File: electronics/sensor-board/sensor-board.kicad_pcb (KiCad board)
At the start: 0 parts

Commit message: Added libraries to sensor board pcb schematic
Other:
- copper layers 0 -> 2
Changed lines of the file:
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@@
-(kicad_pcb (version 20210722) (generator pcbnew)
+(kicad_pcb (version 20210824) (generator pcbnew)
+  (general
+    (thickness 1.6)
+  )
+  (paper "A4")
+  (layers
+    (0 "F.Cu" signal)
+    (31 "B.Cu" signal)
+    (32 "B.Adhes" user "B.Adhesive")
+    (33 "F.Adhes" user "F.Adhesive")
+    (34 "B.Paste" user)
+    (35 "F.Paste" user)
+    (36 "B.SilkS" user "B.Silkscreen")
+    (37 "F.SilkS" user "F.Silkscreen")
+    (38 "B.Mask" user)
+    (39 "F.Mask" user)
+    (40 "Dwgs.User" user "User.Drawings")
+    (41 "Cmts.User" user "User.Comments")
+    (42 "Eco1.User" user "User.Eco1")
+    (43 "Eco2.User" user "User.Eco2")
+    (44 "Edge.Cuts" user)
+    (45 "Margin" user)
+    (46 "B.CrtYd" user "B.Courtyard")
+    (47 "F.CrtYd" user "F.Courtyard")
+    (48 "B.Fab" user)
+    (49 "F.Fab" user)
+    (50 "User.1" user)
+    (51 "User.2" user)
+    (52 "User.3" user)
+    (53 "User.4" user)
+    (54 "User.5" user)
+    (55 "User.6" user)
+    (56 "User.7" user)
+    (57 "User.8" user)
+    (58 "User.9" user)
+  )
+  (setup
+    (pad_to_mask_clearance 0)
+    (pcbplotparams
+      (layerselection 0x00010fc_ffffffff)
+      (disableapertmacros false)
+      (usegerberextensions false)
+      (usegerberattributes true)
+      (usegerberadvancedattributes true)
+      (creategerberjobfile true)
+      (svguseinch false)
+      (svgprecision 6)
+      (excludeedgelayer true)
+      (plotframeref false)
+      (viasonmask false)
+      (mode 1)
+      (useauxorigin false)
+      (hpglpennumber 1)
+      (hpglpenspeed 20)
+      (hpglpendiameter 15.000000)
+      (dxfpolygonmode true)
+      (dxfimperialunits true)
+      (dxfusepcbnewfont true)
+      (psnegative false)
+      (psa4output false)
+      (plotreference true)
+      (plotvalue true)
+      (plotinvisibletext false)
+      (sketchpadsonfab false)
+      (subtractmaskfromsilk false)
+      (outputformat 1)
+      (mirror false)
+      (drillshape 1)
+      (scaleselection 1)
+      (outputdirectory "")
+    )
+  )
+  (net 0 "")
 )

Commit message: work on sensor-board
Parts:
- added C1: 1uF, Capacitor_SMD:C_0603_1608Metric, F.Cu at (64.9, -87.0)
- added C10: 100nF, Capacitor_SMD:C_0603_1608Metric, F.Cu at (230.6, -32.4)
- added C11: 100nF, Capacitor_SMD:C_0603_1608Metric, F.Cu at (237.2, -24.8)
- added C12: 20pF, Capacitor_SMD:C_0603_1608Metric, F.Cu at (181.7, 95.5)
- added C13: 0.1uF, Capacitor_SMD:C_0603_1608Metric, F.Cu at (-39.4, 22.1)
- added C14: 0.1uF, Capacitor_SMD:C_0603_1608Metric, F.Cu at (-42.3, 93.4)
- added C15: 0.1uF, Capacitor_SMD:C_0603_1608Metric, F.Cu at (-38.2, 22.2)
- added C16: 0.1uF, Capacitor_SMD:C_0603_1608Metric, F.Cu at (-42.6, 94.6)
- added C17: 0.1uF, Capacitor_SMD:C_0603_1608Metric, F.Cu at (-38.1, 167.5)
- added C18: 0.1uF, Capacitor_SMD:C_0603_1608Metric, F.Cu at (-30.2, 42.9)
- added C19: 0.1uF, Capacitor_SMD:C_0603_1608Metric, F.Cu at (-34.6, 118.8)
- added C2: 10nF, Capacitor_SMD:C_0603_1608Metric, F.Cu at (57.4, -80.2)
- added C20: 0.1uF, Capacitor_SMD:C_0603_1608Metric, F.Cu at (-37.3, 168.5)
- added C21: 0.1uF, Capacitor_SMD:C_0603_1608Metric, F.Cu at (-31.4, 42.1)
- added C22: 0.1uF, Capacitor_SMD:C_0603_1608Metric, F.Cu at (-36.1, 117.2)
- added C23: 0.1uF, Capacitor_SMD:C_0603_1608Metric, F.Cu at (-38.1, 65.0)
- added C24: 0.1uF, Capacitor_SMD:C_0603_1608Metric, F.Cu at (-36.8, 141.4)
- added C25: 0.1uF, Capacitor_SMD:C_0603_1608Metric, F.Cu at (-39.3, 65.0)
- added C26: 0.1uF, Capacitor_SMD:C_0603_1608Metric, F.Cu at (-39.0, 141.4)
- added C27: 20pF, Capacitor_SMD:C_0603_1608Metric, F.Cu at (175.1, 101.0)
- added C28: 100nF, Capacitor_SMD:C_0603_1608Metric, F.Cu at (160.2, 53.9)
- added C29: 100nF, Capacitor_SMD:C_0603_1608Metric, F.Cu at (245.2, -24.1)
- added C3: 1uF, Capacitor_SMD:C_0603_1608Metric, F.Cu at (64.8, -80.0)
- added C6: 100nF, Capacitor_SMD:C_0603_1608Metric, F.Cu at (201.7, -32.7)
- added C7: 100nF, Capacitor_SMD:C_0603_1608Metric, F.Cu at (214.6, -31.9)
- added C8: 100nF, Capacitor_SMD:C_0603_1608Metric, F.Cu at (164.4, 147.2)
- added C9: 100nF, Capacitor_SMD:C_0603_1608Metric, F.Cu at (223.1, -30.6)
- added J1: SWD Header, Connector_PinHeader_2.54mm:PinHeader_1x04_P2.54mm_Vertical, F.Cu at (305.6, -41.4)
- added J10: Suppply_5V, Connector_PinHeader_2.54mm:PinHeader_1x02_P2.54mm_Horizontal, F.Cu at (79.5, -82.9)
- added J11: Pressure_1, Connector_PinHeader_2.54mm:PinHeader_1x02_P2.54mm_Horizontal, F.Cu at (199.5, 360.1)
- added J12: Pressure_2, Connector_PinHeader_2.54mm:PinHeader_1x02_P2.54mm_Horizontal, F.Cu at (189.3, 360.6)
- added J13: Pressure_3, Connector_PinHeader_2.54mm:PinHeader_1x02_P2.54mm_Horizontal, F.Cu at (179.7, 361.2)
- added J14: Pressure_4, Connector_PinHeader_2.54mm:PinHeader_1x02_P2.54mm_Horizontal, F.Cu at (168.6, 362.4)
- added J15: Pressure_9, Connector_PinHeader_2.54mm:PinHeader_1x02_P2.54mm_Horizontal, F.Cu at (110.0, 366.5)
- added J16: Flow_1, Connector_PinHeader_2.54mm:PinHeader_1x04_P2.54mm_Horizontal, F.Cu at (66.5, 365.6)
- added J17: Flow_2, Connector_PinHeader_2.54mm:PinHeader_1x04_P2.54mm_Horizontal, F.Cu at (93.5, 364.6)
- added J18: CAN_Bus, Resistor_THT:R_Axial_DIN0204_L3.6mm_D1.6mm_P1.90mm_Vertical, F.Cu at (324.9, 28.0)
- added J19: Spare_1, Connector_PinHeader_2.54mm:PinHeader_1x02_P2.54mm_Horizontal, F.Cu at (268.7, 356.6)
- added J2: Supply_24V, Connector_PinHeader_2.54mm:PinHeader_1x02_P2.54mm_Horizontal, F.Cu at (88.4, -34.7)
- added J20: Spare_2, Connector_PinHeader_2.54mm:PinHeader_1x02_P2.54mm_Horizontal, F.Cu at (252.9, 358.1)
- added J21: Spare_3, Connector_PinHeader_2.54mm:PinHeader_1x02_P2.54mm_Horizontal, F.Cu at (236.7, 359.6)
- added J22: Spare_4, Connector_PinHeader_2.54mm:PinHeader_1x02_P2.54mm_Horizontal, F.Cu at (223.0, 361.2)
- added J23: Therm_1, K_type_thermo_conn_F:K_type_thermo_conn_F, F.Cu at (-62.7, 20.7)
- added J24: Therm_4, K_type_thermo_conn_F:K_type_thermo_conn_F, F.Cu at (-62.4, 93.3)
- added J25: Therm_7, K_type_thermo_conn_F:K_type_thermo_conn_F, F.Cu at (-62.4, 169.5)
- added J26: Therm_2, K_type_thermo_conn_F:K_type_thermo_conn_F, F.Cu at (-62.4, 42.5)
- added J27: Therm_5, K_type_thermo_conn_F:K_type_thermo_conn_F, F.Cu at (-62.4, 118.7)
- added J28: Therm_3, K_type_thermo_conn_F:K_type_thermo_conn_F, F.Cu at (-61.4, 67.9)
- added J29: Therm_6, K_type_thermo_conn_F:K_type_thermo_conn_F, F.Cu at (-62.4, 144.1)
- added J3: Supply_12V, Connector_PinHeader_2.54mm:PinHeader_1x02_P2.54mm_Horizontal, F.Cu at (85.4, -57.3)
- added J30: Spare_HR, Connector_PinHeader_2.54mm:PinHeader_1x04_P2.54mm_Horizontal, F.Cu at (450.2, 241.1)
- added J4: Load_C_1, Connector_PinHeader_2.54mm:PinHeader_1x04_P2.54mm_Horizontal, F.Cu at (443.0, 163.0)
- added J5: Load_C_2, Connector_PinHeader_2.54mm:PinHeader_1x04_P2.54mm_Horizontal, F.Cu at (436.7, 202.7)
- added J6: Pressure_5, Connector_PinHeader_2.54mm:PinHeader_1x02_P2.54mm_Horizontal, F.Cu at (159.3, 363.2)
- added J7: Pressure_6, Connector_PinHeader_2.54mm:PinHeader_1x02_P2.54mm_Horizontal, F.Cu at (149.0, 363.8)
- added J8: Pressure_7, Connector_PinHeader_2.54mm:PinHeader_1x02_P2.54mm_Horizontal, F.Cu at (137.3, 364.9)
- added J9: Pressure_8, Connector_PinHeader_2.54mm:PinHeader_1x02_P2.54mm_Horizontal, F.Cu at (123.1, 364.8)
- added L1: 10uH, Inductor_SMD:L_0603_1608Metric, F.Cu at (156.8, 147.4)
- added R10: 100, Resistor_SMD:R_0603_1608Metric, F.Cu at (-41.6, 22.8)
- added R100: 150, Resistor_SMD:R_0603_1608Metric, F.Cu at (87.3, 356.7)
- added R101: NO_RES, Resistor_SMD:R_0603_1608Metric, F.Cu at (33.2, 336.4)
- added R102: 150, Resistor_SMD:R_0603_1608Metric, F.Cu at (106.1, 357.0)
- added R103: 150, Resistor_SMD:R_0603_1608Metric, F.Cu at (64.1, 348.0)
- added R104: 150, Resistor_SMD:R_0603_1608Metric, F.Cu at (87.5, 346.4)
- added R105: NO_RES, Resistor_SMD:R_0603_1608Metric, F.Cu at (39.5, 327.5)
- added R106: NO_RES, Resistor_SMD:R_0603_1608Metric, F.Cu at (43.4, 342.7)
- added R107: NO_RES, Resistor_SMD:R_0603_1608Metric, F.Cu at (37.1, 321.0)
- added R108: TO CALCULATE 4.7k, Resistor_SMD:R_0603_1608Metric, F.Cu at (321.4, 80.5)
- added R109: 100, Resistor_SMD:R_0603_1608Metric, F.Cu at (317.4, 83.0)
- added R11: 100, Resistor_SMD:R_0603_1608Metric, F.Cu at (-40.5, 94.5)
- added R110: 100, Resistor_SMD:R_0603_1608Metric, F.Cu at (325.4, 77.9)
- added R111: 10k, Resistor_SMD:R_0603_1608Metric, F.Cu at (164.1, 121.9)
- added R112: 0k, Resistor_SMD:R_0603_1608Metric, F.Cu at (168.7, 104.6)
- added R12: 100, Resistor_SMD:R_0603_1608Metric, F.Cu at (-41.6, 94.1)
- added R13: 10k, Resistor_SMD:R_0603_1608Metric, F.Cu at (-41.3, 93.6)
- added R14: 7.5k, Resistor_SMD:R_0603_1608Metric, F.Cu at (-42.1, 93.8)
- added R15: 2M, Resistor_SMD:R_0603_1608Metric, F.Cu at (-38.7, 168.3)
- added R16: 2M, Resistor_SMD:R_0603_1608Metric, F.Cu at (-38.3, 168.8)
- added R17: 1M, Resistor_SMD:R_0603_1608Metric, F.Cu at (-38.7, 167.9)
- added R18: 100, Resistor_SMD:R_0603_1608Metric, F.Cu at (-39.7, 168.5)
- added R19: 100, Resistor_SMD:R_0603_1608Metric, F.Cu at (-39.3, 169.2)
- added R2: TO CALCULATE 4.7k, Resistor_SMD:R_0603_1608Metric, F.Cu at (315.4, 73.8)
- added R20: 2M, Resistor_SMD:R_0603_1608Metric, F.Cu at (-31.6, 41.7)
- added R21: 2M, Resistor_SMD:R_0603_1608Metric, F.Cu at (-36.1, 117.8)
- added R22: 2M, Resistor_SMD:R_0603_1608Metric, F.Cu at (-30.6, 42.0)
- added R23: 2M, Resistor_SMD:R_0603_1608Metric, F.Cu at (-36.7, 117.2)
- added R24: 1M, Resistor_SMD:R_0603_1608Metric, F.Cu at (-30.8, 41.5)
- added R25: 1M, Resistor_SMD:R_0603_1608Metric, F.Cu at (-36.7, 117.6)
- added R26: 100, Resistor_SMD:R_0603_1608Metric, F.Cu at (-32.1, 41.9)
- added R27: 100, Resistor_SMD:R_0603_1608Metric, F.Cu at (-30.6, 42.4)
- added R28: 100, Resistor_SMD:R_0603_1608Metric, F.Cu at (-37.5, 116.3)
- added R29: 100, Resistor_SMD:R_0603_1608Metric, F.Cu at (-35.9, 118.8)
- added R3: 2M, Resistor_SMD:R_0603_1608Metric, F.Cu at (-35.9, 22.3)
- added R30: 10k, Resistor_SMD:R_0603_1608Metric, F.Cu at (-39.1, 167.7)
- added R31: 43k, Resistor_SMD:R_0603_1608Metric, F.Cu at (-40.8, 166.6)
- added R32: 10k, Resistor_SMD:R_0603_1608Metric, F.Cu at (-30.8, 42.7)
- added R33: 10k, Resistor_SMD:R_0603_1608Metric, F.Cu at (-36.8, 116.2)
- added R34: 2.2k, Resistor_SMD:R_0603_1608Metric, F.Cu at (-31.5, 42.1)
- added R35: 13k, Resistor_SMD:R_0603_1608Metric, F.Cu at (-36.8, 116.2)
- added R36: 2M, Resistor_SMD:R_0603_1608Metric, F.Cu at (-40.1, 64.9)
- added R37: 2M, Resistor_SMD:R_0603_1608Metric, F.Cu at (-36.5, 140.5)
- added R38: 2M, Resistor_SMD:R_0603_1608Metric, F.Cu at (-39.6, 64.8)
- added R39: 2M, Resistor_SMD:R_0603_1608Metric, F.Cu at (-37.7, 143.1)
- added R4: 2M, Resistor_SMD:R_0603_1608Metric, F.Cu at (-42.4, 94.1)
- added R40: 1M, Resistor_SMD:R_0603_1608Metric, F.Cu at (-39.6, 64.5)
- added R41: 1M, Resistor_SMD:R_0603_1608Metric, F.Cu at (-37.4, 142.2)
- added R42: 100, Resistor_SMD:R_0603_1608Metric, F.Cu at (-39.1, 64.4)
- added R43: 100, Resistor_SMD:R_0603_1608Metric, F.Cu at (-39.9, 65.5)
- added R44: 100, Resistor_SMD:R_0603_1608Metric, F.Cu at (-39.4, 140.5)
- added R45: 100, Resistor_SMD:R_0603_1608Metric, F.Cu at (-38.8, 143.4)
- added R46: 10k, Resistor_SMD:R_0603_1608Metric, F.Cu at (-37.6, 64.9)
- added R47: 10k, Resistor_SMD:R_0603_1608Metric, F.Cu at (-38.2, 142.2)
- added R48: 4.3k, Resistor_SMD:R_0603_1608Metric, F.Cu at (-40.4, 63.9)
- added R49: 22k, Resistor_SMD:R_0603_1608Metric, F.Cu at (-39.6, 142.8)
- added R5: 2M, Resistor_SMD:R_0603_1608Metric, F.Cu at (-39.2, 22.4)
- added R50: NO_RES, Resistor_SMD:R_0603_1608Metric, F.Cu at (269.4, 349.2)
- added R51: NO_RES, Resistor_SMD:R_0603_1608Metric, F.Cu at (264.3, 350.7)
- added R52: NO_RES, Resistor_SMD:R_0603_1608Metric, F.Cu at (254.5, 346.9)
- added R53: NO_RES, Resistor_SMD:R_0603_1608Metric, F.Cu at (250.2, 349.8)
- added R54: NO_RES, Resistor_SMD:R_0603_1608Metric, F.Cu at (238.2, 349.7)
- added R55: NO_RES, Resistor_SMD:R_0603_1608Metric, F.Cu at (233.4, 352.9)
- added R56: NO_RES, Resistor_SMD:R_0603_1608Metric, F.Cu at (224.4, 353.2)
- added R57: NO_RES, Resistor_SMD:R_0603_1608Metric, F.Cu at (220.2, 352.9)
- added R58: NO_RES, Resistor_SMD:R_0603_1608Metric, F.Cu at (264.0, 340.8)
- added R59: NO_RES, Resistor_SMD:R_0603_1608Metric, F.Cu at (249.7, 336.0)
- added R6: 2M, Resistor_SMD:R_0603_1608Metric, F.Cu at (-41.3, 94.7)
- added R60: NO_RES, Resistor_SMD:R_0603_1608Metric, F.Cu at (233.6, 340.9)
- added R61: NO_RES, Resistor_SMD:R_0603_1608Metric, F.Cu at (220.7, 339.9)
- added R62: NO_RES, Resistor_SMD:R_0603_1608Metric, F.Cu at (231.4, 302.6)
- added R63: NO_RES, Resistor_SMD:R_0603_1608Metric, F.Cu at (244.3, 318.6)
- added R64: NO_RES, Resistor_SMD:R_0603_1608Metric, F.Cu at (234.6, 314.8)
- added R65: NO_RES, Resistor_SMD:R_0603_1608Metric, F.Cu at (219.0, 308.2)
- added R66: 100, Resistor_SMD:R_0603_1608Metric, F.Cu at (425.0, 208.4)
- added R67: 24.92, Resistor_SMD:R_0603_1608Metric, F.Cu at (425.8, 200.5)
- added R68: 100, Resistor_SMD:R_0603_1608Metric, F.Cu at (430.6, 167.1)
- added R69: 24.92, Resistor_SMD:R_0603_1608Metric, F.Cu at (425.2, 163.2)
- added R7: 1M, Resistor_SMD:R_0603_1608Metric, F.Cu at (-31.2, 22.3)
- added R70: 100, Resistor_SMD:R_0603_1608Metric, F.Cu at (417.4, 255.7)
- added R71: 24.92, Resistor_SMD:R_0603_1608Metric, F.Cu at (423.3, 248.1)
- added R72: 100, Resistor_SMD:R_0603_1608Metric, F.Cu at (422.8, 326.6)
- added R73: 24.92, Resistor_SMD:R_0603_1608Metric, F.Cu at (425.5, 347.3)
- added R74: 82500, Resistor_SMD:R_0603_1608Metric, F.Cu at (431.1, 206.7)
- added R75: 82500, Resistor_SMD:R_0603_1608Metric, F.Cu at (430.0, 257.6)
- added R76: 82500, Resistor_SMD:R_0603_1608Metric, F.Cu at (416.2, 171.4)
- added R77: 82500, Resistor_SMD:R_0603_1608Metric, F.Cu at (431.4, 343.5)
- added R78: 82500, Resistor_SMD:R_0603_1608Metric, F.Cu at (414.5, 161.6)
- added R79: 82500, Resistor_SMD:R_0603_1608Metric, F.Cu at (409.3, 205.4)
- added R8: 1M, Resistor_SMD:R_0603_1608Metric, F.Cu at (-42.0, 93.6)
- added R80: 82500, Resistor_SMD:R_0603_1608Metric, F.Cu at (431.3, 243.3)
- added R81: 82500, Resistor_SMD:R_0603_1608Metric, F.Cu at (402.4, 339.2)
- added R82: 150, Resistor_SMD:R_0603_1608Metric, F.Cu at (195.3, 354.5)
- added R83: 150, Resistor_SMD:R_0603_1608Metric, F.Cu at (185.9, 355.8)
- added R84: 150, Resistor_SMD:R_0603_1608Metric, F.Cu at (175.9, 355.0)
- added R85: 150, Resistor_SMD:R_0603_1608Metric, F.Cu at (165.5, 358.8)
- added R86: 150, Resistor_SMD:R_0603_1608Metric, F.Cu at (195.3, 342.5)
- added R87: 150, Resistor_SMD:R_0603_1608Metric, F.Cu at (186.0, 346.2)
- added R88: 150, Resistor_SMD:R_0603_1608Metric, F.Cu at (175.2, 346.4)
- added R89: 150, Resistor_SMD:R_0603_1608Metric, F.Cu at (165.9, 347.3)
- added R9: 100, Resistor_SMD:R_0603_1608Metric, F.Cu at (-39.7, 21.8)
- added R90: 150, Resistor_SMD:R_0603_1608Metric, F.Cu at (156.6, 356.0)
- added R91: 150, Resistor_SMD:R_0603_1608Metric, F.Cu at (146.7, 356.1)
- added R92: 150, Resistor_SMD:R_0603_1608Metric, F.Cu at (134.4, 357.9)
- added R93: 150, Resistor_SMD:R_0603_1608Metric, F.Cu at (120.3, 359.8)
- added R94: 150, Resistor_SMD:R_0603_1608Metric, F.Cu at (156.1, 348.5)
- added R95: 150, Resistor_SMD:R_0603_1608Metric, F.Cu at (146.3, 346.8)
- added R96: 150, Resistor_SMD:R_0603_1608Metric, F.Cu at (134.3, 349.6)
- added R97: 150, Resistor_SMD:R_0603_1608Metric, F.Cu at (120.0, 353.0)
- added R98: 150, Resistor_SMD:R_0603_1608Metric, F.Cu at (106.9, 362.8)
- added R99: 150, Resistor_SMD:R_0603_1608Metric, F.Cu at (61.2, 356.4)
- added SW1: SW_Push_Dual, Custom_button_CS1102:Button CS1102, F.Cu at (144.6, 52.1)
- added U1: LD3985M33R_SOT23, Package_TO_SOT_SMD:SOT-23-5, F.Cu at (61.1, -84.8)
- added U10: MCP96RL01T, MCP96RL01T:MCP96RL01T_QFN, F.Cu at (-38.8, 142.2)
- added U11: LMC6036, LMC6036:SOP65P640X120-14N, F.Cu at (89.0, 329.6)
- added U12: LMC6036, LMC6036:SOP65P640X120-14N, F.Cu at (138.4, 335.4)
- added U13: LMC6036, LMC6036:SOP65P640X120-14N, F.Cu at (178.8, 331.1)
- added U14: MAX44252ASD, MAX44252ASD-:MAX44252ASD&plus_, F.Cu at (347.5, 201.2)
- added U15: LMC6036, LMC6036:SOP65P640X120-14N, F.Cu at (226.3, 319.2)
- added U2: MAX33012EASA+, MAX33012EASA+:MAX33012EASA+, F.Cu at (316.9, 24.0)
- added U3: STM32F105VBH6, STM32F105VBH6:STM32F105VBH6, F.Cu at (141.9, 94.1)
- added U4: MCP96RL01T, MCP96RL01T:MCP96RL01T_QFN, F.Cu at (-39.4, 22.0)
- added U5: MCP96RL01T, MCP96RL01T:MCP96RL01T_QFN, F.Cu at (-42.0, 93.9)
- added U6: MCP96RL01T, MCP96RL01T:MCP96RL01T_QFN, F.Cu at (-38.8, 168.5)
- added U7: MCP96RL01T, MCP96RL01T:MCP96RL01T_QFN, F.Cu at (-31.5, 42.2)
- added U8: MCP96RL01T, MCP96RL01T:MCP96RL01T_QFN, F.Cu at (-36.7, 117.4)
- added U9: MCP96RL01T, MCP96RL01T:MCP96RL01T_QFN, F.Cu at (-39.5, 64.6)
- added Y1: 25MHz 9pF, Resistor_THT:R_Axial_DIN0204_L3.6mm_D1.6mm_P1.90mm_Vertical, F.Cu at (173.6, 94.8)

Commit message: work on sensor-board pcb
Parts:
- J18: footprint Resistor_THT:R_Axial_DIN0204_L3.6mm_D1.6mm_P1.90mm_Vertical -> Connector_PinHeader_2.54mm:PinHeader_1x02_P2.54mm_Horizontal
- Y1: value 25MHz 9pF -> Crystal_GND24; footprint Resistor_THT:R_Axial_DIN0204_L3.6mm_D1.6mm_P1.90mm_Vertical -> Crystal:Crystal_SMD_3225-4Pin_3.2x2.5mm
- moved R77 569.9 mm to (-119.1, 196.0), turned to 180 degrees
- moved R73 560.5 mm to (-113.1, 192.2), turned to 180 degrees
- moved R72 545.2 mm to (-110.4, 212.8), turned to 180 degrees
- moved R81 511.7 mm to (-90.1, 200.3), turned to 180 degrees
- moved U14 406.5 mm to (-35.2, 338.3), turned to 180 degrees
- moved J30 405.8 mm to (83.2, 68.0), turned to 180 degrees
- moved R75 390.0 mm to (92.1, 62.9)
- moved R80 382.7 mm to (92.1, 66.0), turned to 180 degrees
- moved R71 382.5 mm to (88.7, 62.9), turned to 180 degrees
- moved R70 379.8 mm to (88.3, 66.0), turned to 180 degrees
- moved J5 372.4 mm to (83.2, 85.3), turned to 180 degrees
- moved J4 364.8 mm to (83.2, 102.6), turned to 180 degrees
- moved R74 362.5 mm to (91.4, 80.0)
- moved R66 360.6 mm to (87.0, 82.8), turned to 180 degrees
- moved R67 359.8 mm to (86.8, 79.9), turned to 180 degrees
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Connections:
- Y1 pad 1: Net-(C12-Pad2) -> GND
- Y1 pad 2: Net-(C27-Pad2) -> Net-(C12-Pad2)
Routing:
- net GND: track 0.00 -> 223.1 mm, vias 0 -> 10
- net +3V3: track 0.00 -> 193.9 mm, vias 0 -> 19
- net Net-(J28-Pad2): track 0.00 -> 33.0 mm
- net Net-(J27-Pad2): track 0.00 -> 33.0 mm
- net Net-(J23-Pad2): track 0.00 -> 33.0 mm
- net Net-(J29-Pad2): track 0.00 -> 33.0 mm
- net Net-(J25-Pad2): track 0.00 -> 33.0 mm
- net Net-(J24-Pad2): track 0.00 -> 33.0 mm
- net Net-(J26-Pad2): track 0.00 -> 33.0 mm
- net Net-(J27-Pad1): track 0.00 -> 27.5 mm
- net Net-(J26-Pad1): track 0.00 -> 27.5 mm
- net Net-(J25-Pad1): track 0.00 -> 27.5 mm
- net Net-(J28-Pad1): track 0.00 -> 27.5 mm
- net Net-(J23-Pad1): track 0.00 -> 27.5 mm
- net Net-(J29-Pad1): track 0.00 -> 27.5 mm
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- added copper zone on B.Cu, net GND
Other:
- copper layers 2 -> 4

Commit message: work on sensor-board pcb
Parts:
- removed R101, R105, R106, R107: NO_RES, Resistor_SMD:R_0603_1608Metric
- added J31: Spare_HR_2, Custom_Molex_SL_2.54:SL_2.54_H_4pin, F.Cu at (81.2, 72.4)
- added TP1: TestPoint, TestPoint:TestPoint_Pad_D2.0mm, F.Cu at (181.6, 135.3)
- added TP2: TestPoint, TestPoint:TestPoint_Pad_D2.0mm, F.Cu at (181.8, 129.4)
- added TP3: TestPoint, TestPoint:TestPoint_Pad_D2.0mm, F.Cu at (159.2, 129.4)
- added TP4: TestPoint, TestPoint:TestPoint_Pad_D2.0mm, F.Cu at (159.2, 135.3)
- added TP5: TestPoint, TestPoint:TestPoint_Pad_D2.0mm, F.Cu at (148.6, 103.6)
- added TP6: TestPoint, TestPoint:TestPoint_Pad_D2.0mm, F.Cu at (152.7, 103.6)
- added TP7: TestPoint, TestPoint:TestPoint_Pad_D2.0mm, F.Cu at (156.7, 103.6)
- J10, J11, J12, J13, J14, J15, J18, J19, J2, J20, J21, J22, J3, J6, J7, J8, J9: footprint Connector_PinHeader_2.54mm:PinHeader_1x02_P2.54mm_Horizontal -> Custom_Molex_SL_2.54:SL_2.54_H_2pin
- J16, J17, J4, J5: footprint Connector_PinHeader_2.54mm:PinHeader_1x04_P2.54mm_Horizontal -> Custom_Molex_SL_2.54:SL_2.54_H_4pin
- J30: value Spare_HR -> Spare_HR_1; footprint Connector_PinHeader_2.54mm:PinHeader_1x04_P2.54mm_Horizontal -> Custom_Molex_SL_2.54:SL_2.54_H_4pin
- R108, R2: value TO CALCULATE 4.7k -> 4.7k
- moved R110 303.3 mm to (131.6, 90.7)
- moved R108 302.8 mm to (128.1, 90.8)
- moved R2 296.9 mm to (128.0, 88.8)
- moved R109 295.3 mm to (131.7, 89.0)
- moved J1 293.0 mm to (148.1, 92.7), turned to 90 degrees
- moved U2 288.8 mm to (148.3, 115.6), turned to 180 degrees
- moved U14 272.6 mm to (96.0, 99.3), turned to 90 degrees
- moved R99 244.0 mm to (84.9, 127.6), turned to 180 degrees
- moved R72 241.2 mm to (84.7, 71.1)
- moved J18 238.0 mm to (214.1, 131.7), turned to 90 degrees
- moved R77 236.4 mm to (84.7, 76.2)
- moved R50 234.2 mm to (176.0, 134.5), turned to -90 degrees
- moved R103 232.8 mm to (84.9, 130.1), turned to 180 degrees
- moved R54 231.4 mm to (164.8, 130.2), turned to 90 degrees
- moved R73 230.7 mm to (84.7, 73.7)
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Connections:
- J19 pad 1: +12V -> /SPARE_gen_purp_amp/diff-A
- J20 pad 1: +12V -> /SPARE_gen_purp_amp/diff-B
- J21 pad 1: +12V -> /SPARE_gen_purp_amp/diff-C
- J22 pad 1: +12V -> /SPARE_gen_purp_amp/diff-D
- R108 pad 1: unconnected-(R108-Pad1) -> +3V3
- R2 pad 1: unconnected-(R2-Pad1) -> +3V3
- R62 pad 1: /ADC12_IN14 -> /SPARE_gen_purp_amp/output_A
- U11 pad 12: Net-(R101-Pad1) -> unconnected-(U11-Pad12)
- U11 pad 13: Net-(R106-Pad1) -> unconnected-(U11-Pad13)
- U11 pad 14: /ADC12_IN13 -> /Pressure and Flow/output_D
- U15 pad 1: /ADC12_IN14 -> /SPARE_gen_purp_amp/output_A
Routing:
- net +12V: track 0.00 -> 360.9 mm
- net +24V: track 0.00 -> 171.6 mm
- net /ADC12_IN15: track 0.57 -> 63.3 mm
- net GND: track 223.1 -> 285.5 mm, vias 10 -> 29
- net Net-(R70-Pad1): track 0.00 -> 56.9 mm
- net Net-(R71-Pad1): track 0.00 -> 50.6 mm
- net /Load Cell/output_D: track 0.00 -> 39.4 mm
- net Net-(R72-Pad1): track 0.00 -> 35.5 mm, vias 0 -> 2
- net Net-(R73-Pad1): track 0.00 -> 33.2 mm
- net Net-(R67-Pad1): track 0.00 -> 33.0 mm
- net Net-(R68-Pad1): track 0.00 -> 24.2 mm
- net /ADC12_IN0: track 0.00 -> 24.0 mm
- net Net-(R102-Pad1): track 0.00 -> 22.6 mm
- net /ADC12_IN1: track 0.57 -> 22.8 mm, vias 1 -> 3
- net Net-(R69-Pad1): track 0.00 -> 22.1 mm
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
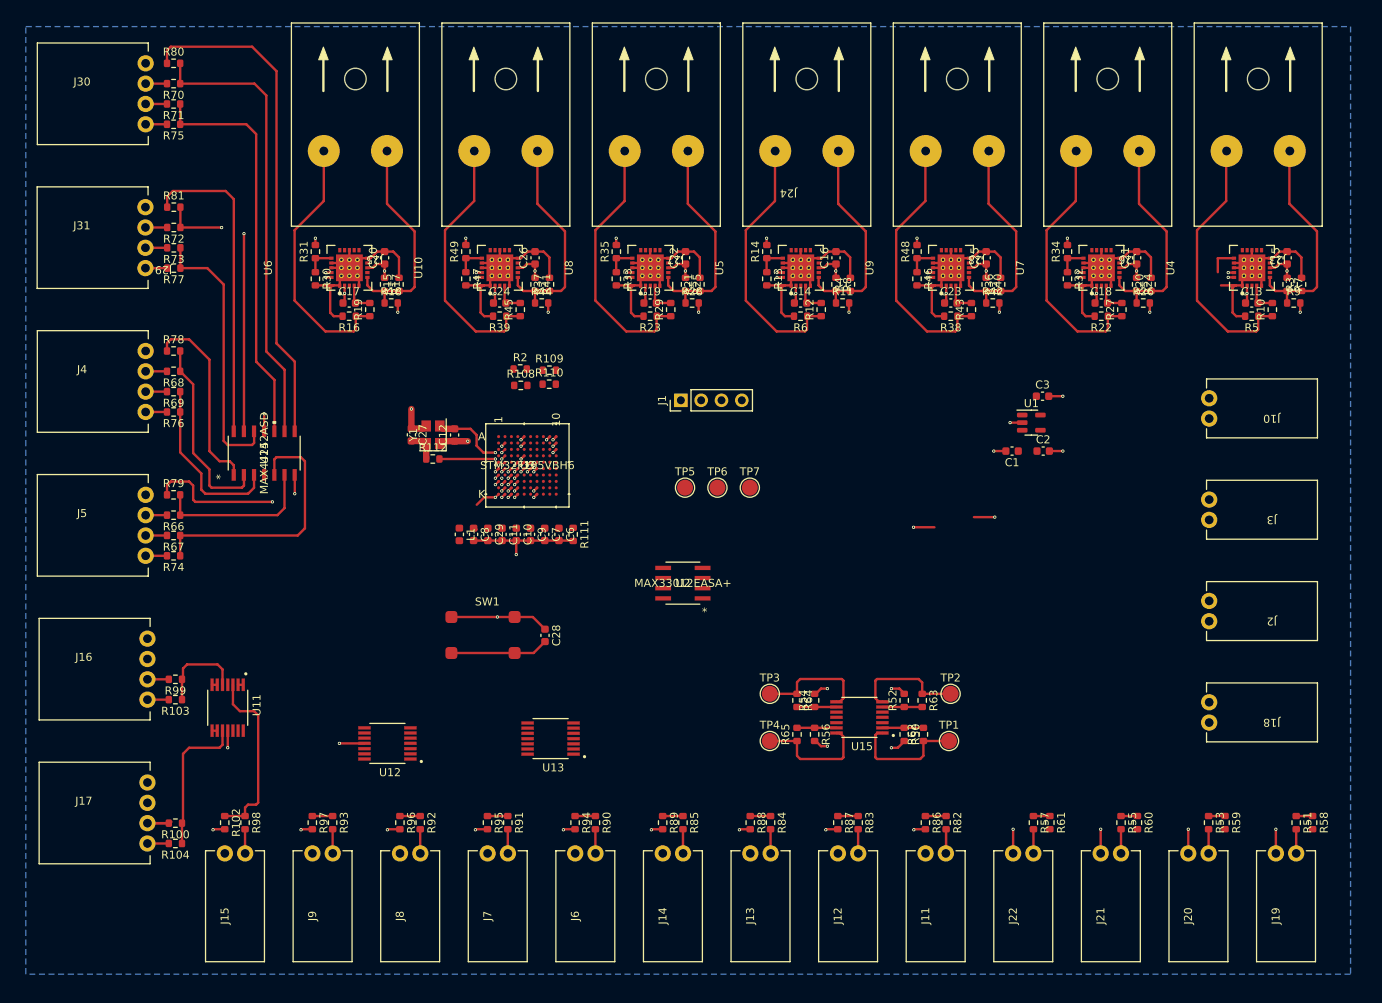
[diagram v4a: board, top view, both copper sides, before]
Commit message: Add SEDS logo to sensor board
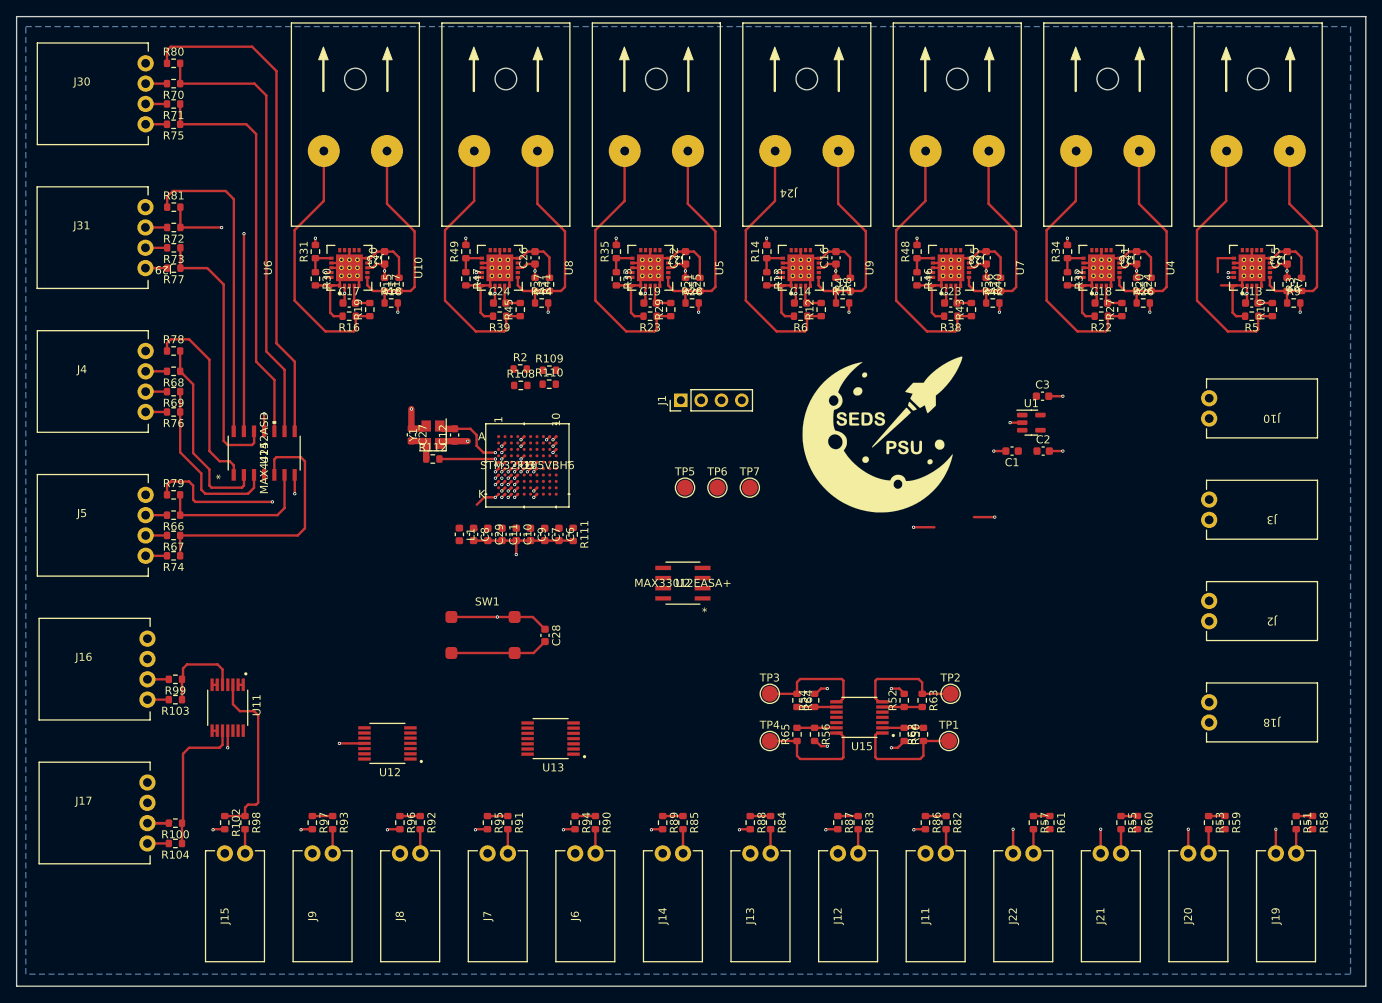
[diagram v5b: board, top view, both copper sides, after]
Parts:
- added Ref**: Val**, CustomFootprints:seds-logo, F.Cu at (173.2, 96.8)
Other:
- board outline added: 168.7 x 121.2 mm

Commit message: work on sensor-board
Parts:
- moved U2 36.6 mm to (184.9, 115.1), turned to 0 degrees
- moved U13 17.0 mm to (148.8, 135.0)
- moved TP2 14.9 mm to (196.3, 125.9)
- moved TP3 14.9 mm to (173.7, 125.9)
- moved R52 14.9 mm to (190.5, 126.7)
- moved R54 14.9 mm to (179.3, 126.7)
- moved R63 14.9 mm to (192.8, 126.7)
- moved R64 14.9 mm to (177.1, 126.7)
- moved U15 14.8 mm to (184.9, 129.5)
- moved TP1 14.7 mm to (196.1, 133.2)
- moved TP4 14.7 mm to (173.7, 133.2)
- moved R50 14.7 mm to (190.5, 132.4)
- moved R56 14.7 mm to (179.3, 132.4)
- moved R62 14.7 mm to (192.9, 132.4)
- moved R65 14.7 mm to (177.1, 132.4)
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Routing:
- net Net-(R51-Pad1): track 2.05 -> 50.5 mm
- net Net-(J18-Pad1): track 0.00 -> 45.6 mm
- net /SPARE_gen_purp_amp/diff-B: track 4.92 -> 50.3 mm
- net /SPARE_gen_purp_amp/diff-A: track 5.00 -> 50.3 mm
- net Net-(R53-Pad1): track 2.05 -> 46.2 mm
- net /SPARE_gen_purp_amp/diff-C: track 4.89 -> 42.8 mm
- net Net-(J18-Pad2): track 0.00 -> 35.6 mm
- net Net-(R55-Pad1): track 2.05 -> 36.0 mm
- net Net-(R82-Pad1): track 2.58 -> 34.6 mm
- net Net-(R90-Pad1): track 2.54 -> 34.4 mm
- net Net-(R83-Pad1): track 2.54 -> 29.7 mm
- net Net-(R91-Pad1): track 2.54 -> 28.2 mm
- net Net-(R57-Pad1): track 2.05 -> 24.5 mm
- net +5V: track 0.00 -> 21.7 mm
- net /SPARE_gen_purp_amp/diff-D: track 4.89 -> 24.4 mm
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
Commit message: work on sensor-board
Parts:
- removed Ref**: Val**, CustomFootprints:seds-logo
- removed TP7: TestPoint, TestPoint:TestPoint_Pad_D2.0mm
- U2: value MAX33012EASA+ -> 21-0041-3-M_90-0096-8L_MXM
- moved J1 31.3 mm to (184.0, 92.6), turned to 0 degrees
- moved TP5 11.1 mm to (160.7, 121.2)
- moved TP6 7.24 mm to (156.6, 121.2)
- moved C27 3.49 mm to (113.5, 93.7)
- moved R112 3.49 mm to (116.2, 96.7)
- moved C12 3.49 mm to (118.9, 93.7)
- moved Y1 3.49 mm to (116.2, 93.7)
- moved C10 1.55 mm to (127.5, 111.0)
- moved C11 1.55 mm to (125.7, 111.0)
- moved C29 1.55 mm to (124.0, 111.0)
- moved C6 1.55 mm to (132.8, 111.0)
- moved C7 1.55 mm to (131.1, 111.0)
- moved C8 1.55 mm to (122.2, 111.0)
- moved C9 1.55 mm to (129.3, 111.0)
- moved L1 1.55 mm to (120.4, 111.0)
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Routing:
- net +3V3: track 203.1 -> 574.2 mm, vias 22 -> 39
- net /I2C1_SDA: track 4.90 -> 154.2 mm, vias 7 -> 8
- net /I2C1_SCL: track 4.90 -> 145.8 mm, vias 7 -> 10
- net /ADC12_IN12: track 3.00 -> 101.2 mm
- net /ADC12_IN11: track 3.08 -> 86.5 mm, vias 2 -> 3
- net /ADC12_IN15: track 63.3 -> 142.6 mm, vias 1 -> 3
- net /CAN_RX: track 0.57 -> 65.2 mm, vias 1 -> 2
- net /CAN_TX: track 0.57 -> 62.9 mm, vias 1 -> 2
- net /ADC12_IN6: track 3.08 -> 63.1 mm
- net /ADC12_IN3: track 3.08 -> 60.1 mm
- net /ADC12_IN13: track 0.57 -> 56.4 mm, vias 1 -> 2
- net /ADC12_IN10: track 3.08 -> 57.6 mm
- net /SWCLK: track 0.57 -> 54.6 mm
- net /SWDIO: track 0.57 -> 53.5 mm
- net /ADC12_IN4: track 3.08 -> 54.5 mm, vias 2 -> 4
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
